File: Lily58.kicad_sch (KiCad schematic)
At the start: 30 parts, among them J1 USB_C_Receptacle, J2 USB_C_Receptacle, Q1 2N7002, Q2 2N7002, Q3 2N7002, Q4 2N7002, U1 ESP32-S3-WROOM-2, U2 TPS63001, U3 BQ24090DGQ, Y1 Crystal_GND24

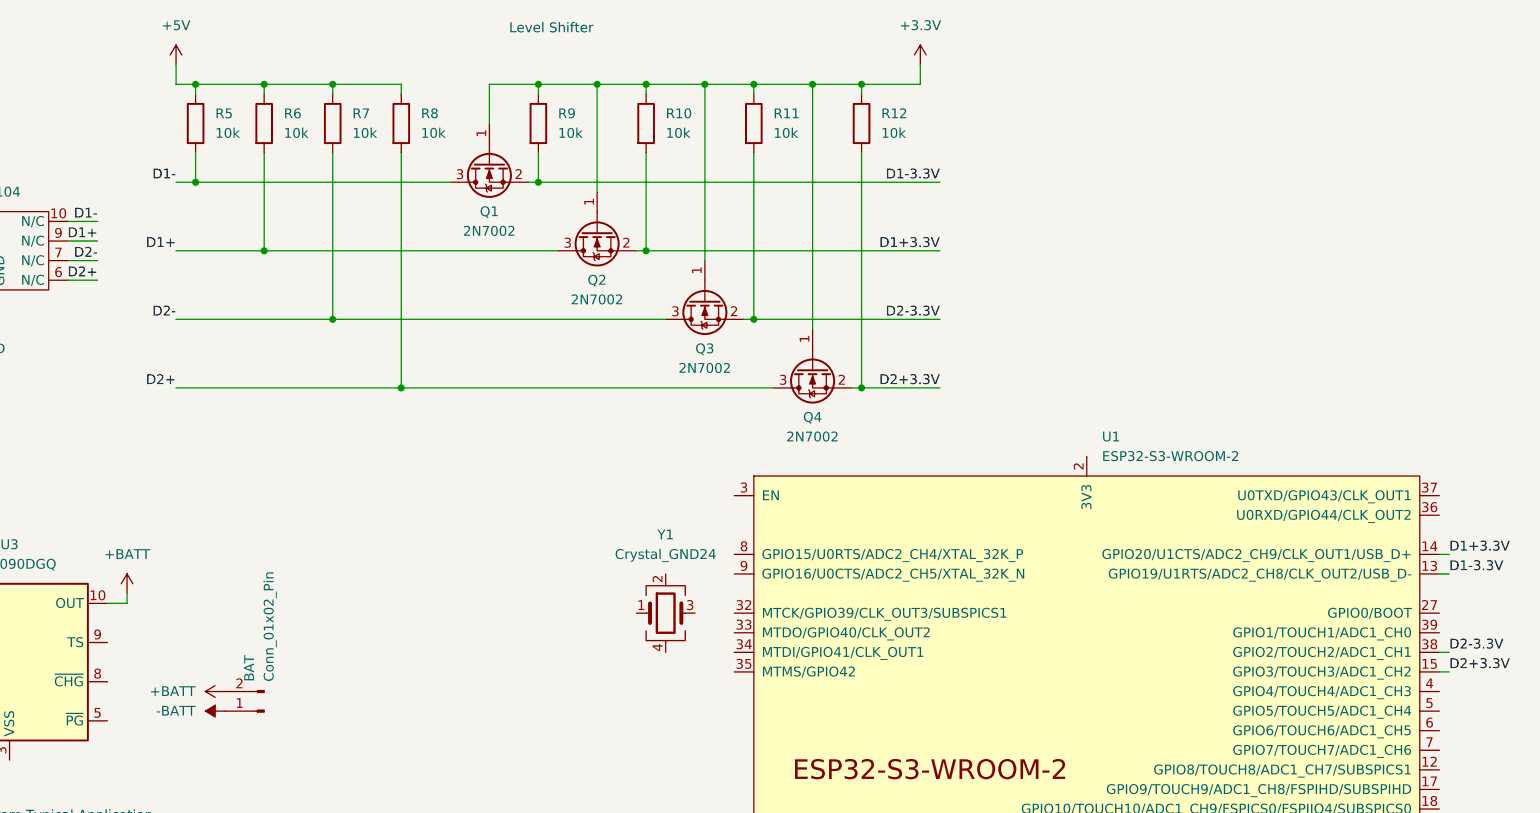
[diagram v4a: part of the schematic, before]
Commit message: removed unnecessary level shifter since data lines are 3V3 already
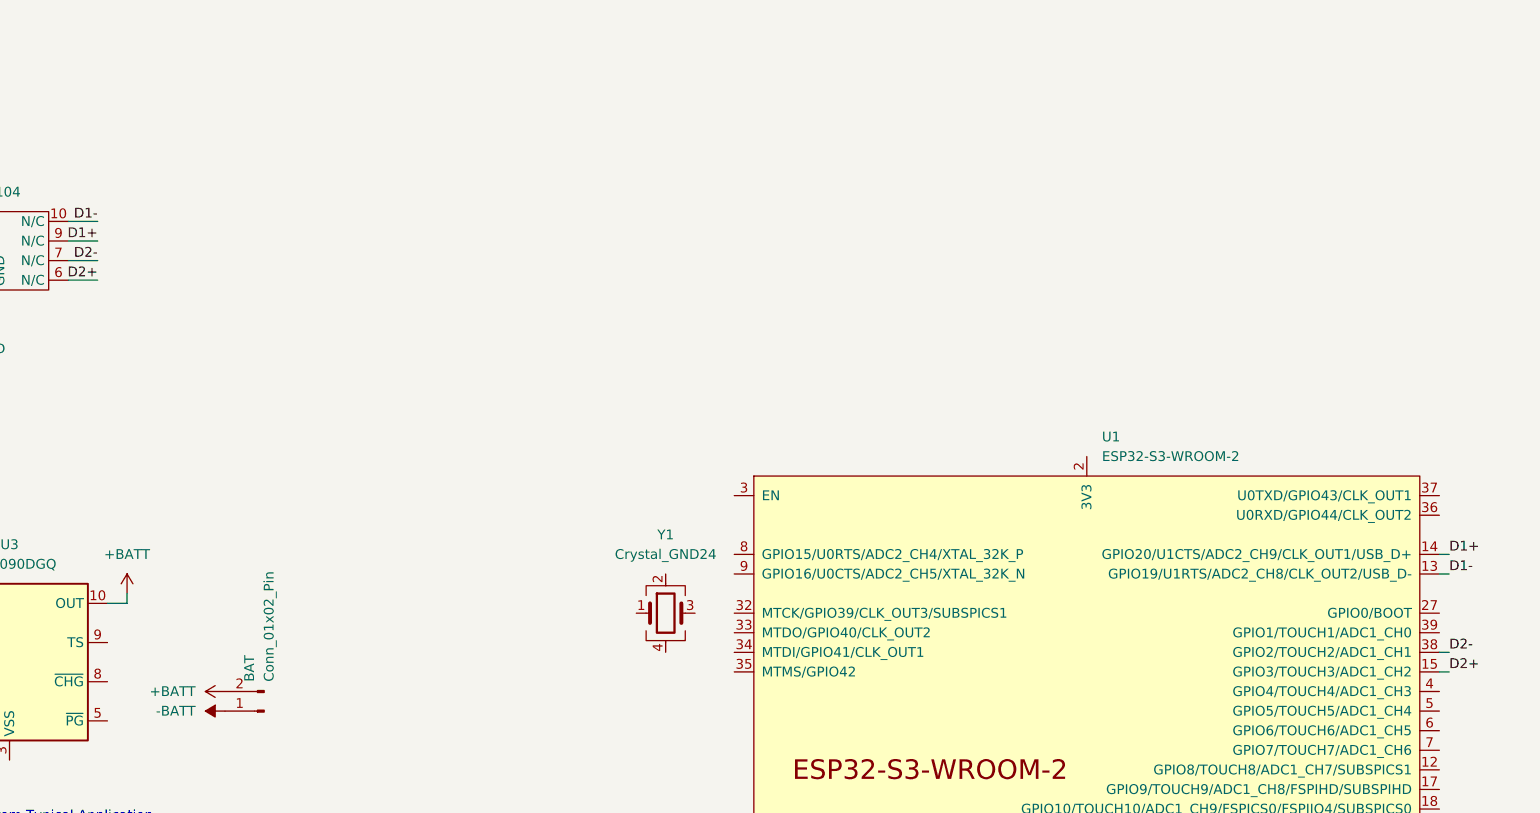
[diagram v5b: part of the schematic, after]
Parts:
- removed Q1, Q2, Q3, Q4: 2N7002, Package_TO_SOT_SMD:SOT-23, symbol Transistor_FET:2N7002
- removed R10, R11, R12, R5, R6, R7, R8, R9: 10k, symbol Device:R
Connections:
- net D1+3.3V is gone; now on net D1+: U1.14 (GPIO20/U1CTS/ADC2_CH9/CLK_OUT1/USB_D+)
- net D1-3.3V is gone; now on net D1-: U1.13 (GPIO19/U1RTS/ADC2_CH8/CLK_OUT2/USB_D-)
- net D2+3.3V is gone; now on net D2+: U1.15 (GPIO3/TOUCH3/ADC1_CH2)
- net D2-3.3V is gone; now on net D2-: U1.38 (GPIO2/TOUCH2/ADC1_CH1)
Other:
- note removed: "Level Shifter"

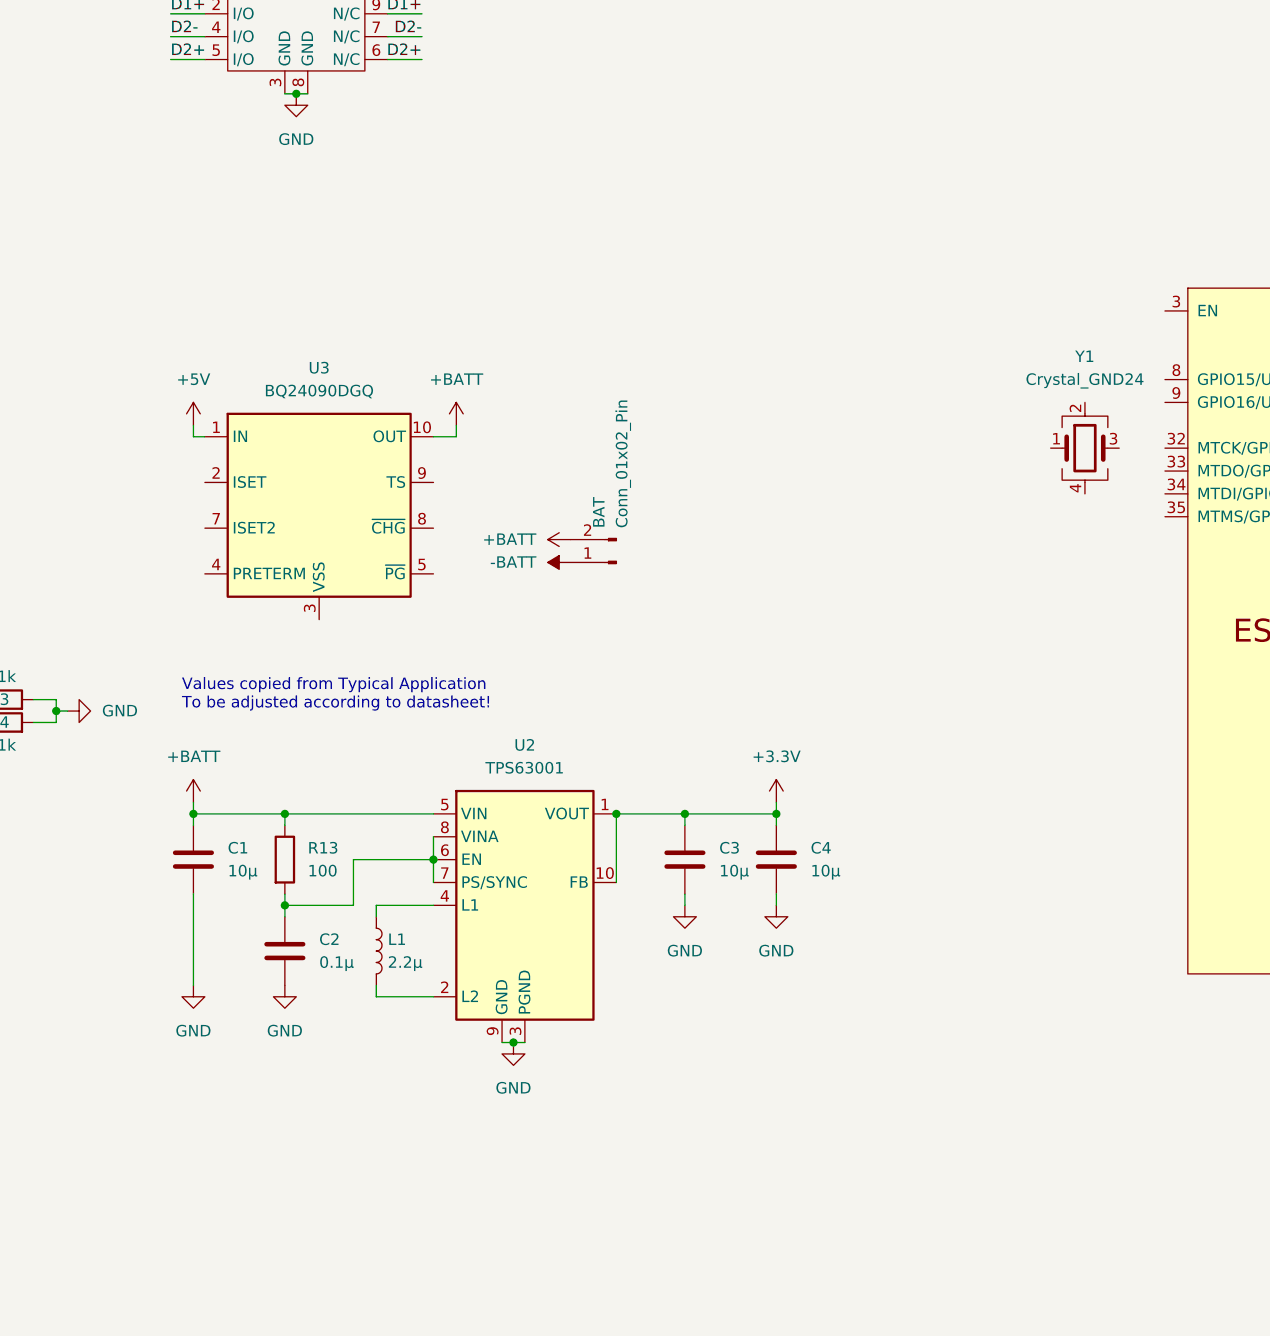
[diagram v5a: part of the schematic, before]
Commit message: added buck-boost-converters and corrected passive components
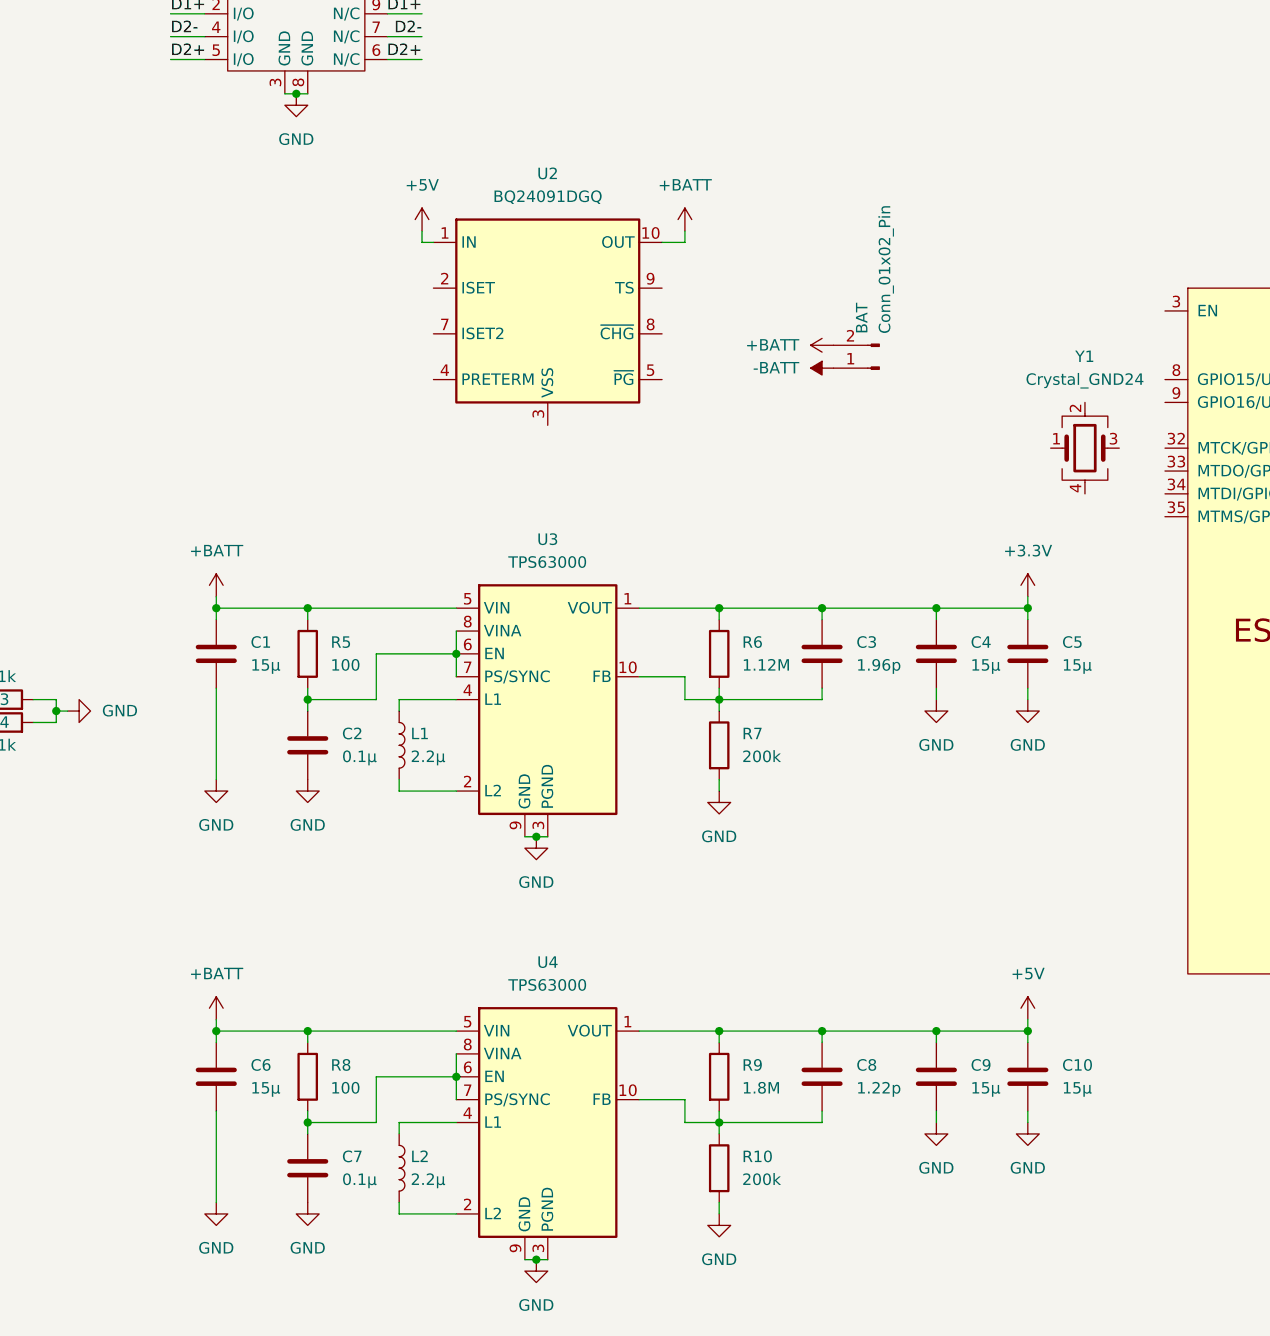
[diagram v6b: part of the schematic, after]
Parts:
- removed R13: 100, symbol Device:R
- added C10, C6, C9: 15µ, symbol Device:C
- added C3: 1.96p, symbol Device:C
- added C7: 0.1µ, symbol Device:C
- added C8: 1.22p, symbol Device:C
- added L2: 2.2µ, symbol Device:L
- added R10, R7: 200k, symbol Device:R
- added R5, R8: 100, symbol Device:R
- added R6: 1.12M, symbol Device:R
- added R9: 1.8M, symbol Device:R
- added U4: TPS63000, Package_SON:Texas_DRC0010J_ThermalVias, symbol Regulator_Switching:TPS63001
- C1: value 10µ -> 15µ
- C4: renamed from C3; value 10µ -> 15µ
- C5: renamed from C4; value 10µ -> 15µ
- U2: renamed from U3; value BQ24090DGQ -> BQ24091DGQ
- U3: renamed from U2; value TPS63001 -> TPS63000
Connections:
- net +3.3V: now also C3.1, R6.1; no longer U3.10 (FB)
- net +5V: now also C10.1, C8.1, C9.1, R9.1, U4.1 (VOUT)
- net +BATT: now also C6.1, R5.1, R8.1, U4.5 (VIN)
- net GND: now also C10.2, C6.2, C7.2, C9.2, R10.2, R7.2, U4.11 (PGND), U4.3 (PGND), U4.9 (GND)
- net at C2.1, U3.6 (EN), U3.7 (PS/SYNC)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: now also R5.2
- new net: L2.1, U4.4 (L1)
- new net: L2.2, U4.2 (L2)
- new net: C8.2, R10.1, R9.2, U4.10 (FB)
- new net: C7.1, R8.2, U4.6 (EN), U4.7 (PS/SYNC), U4.8 (VINA)
- new net: C3.2, R6.2, R7.1, U3.10 (FB)
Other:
- note removed: "Values copied from Typical Application To be adjusted according to datasheet!"
- moved on the sheet: BAT, C1, C2, C4, C5, L1, U2, U3

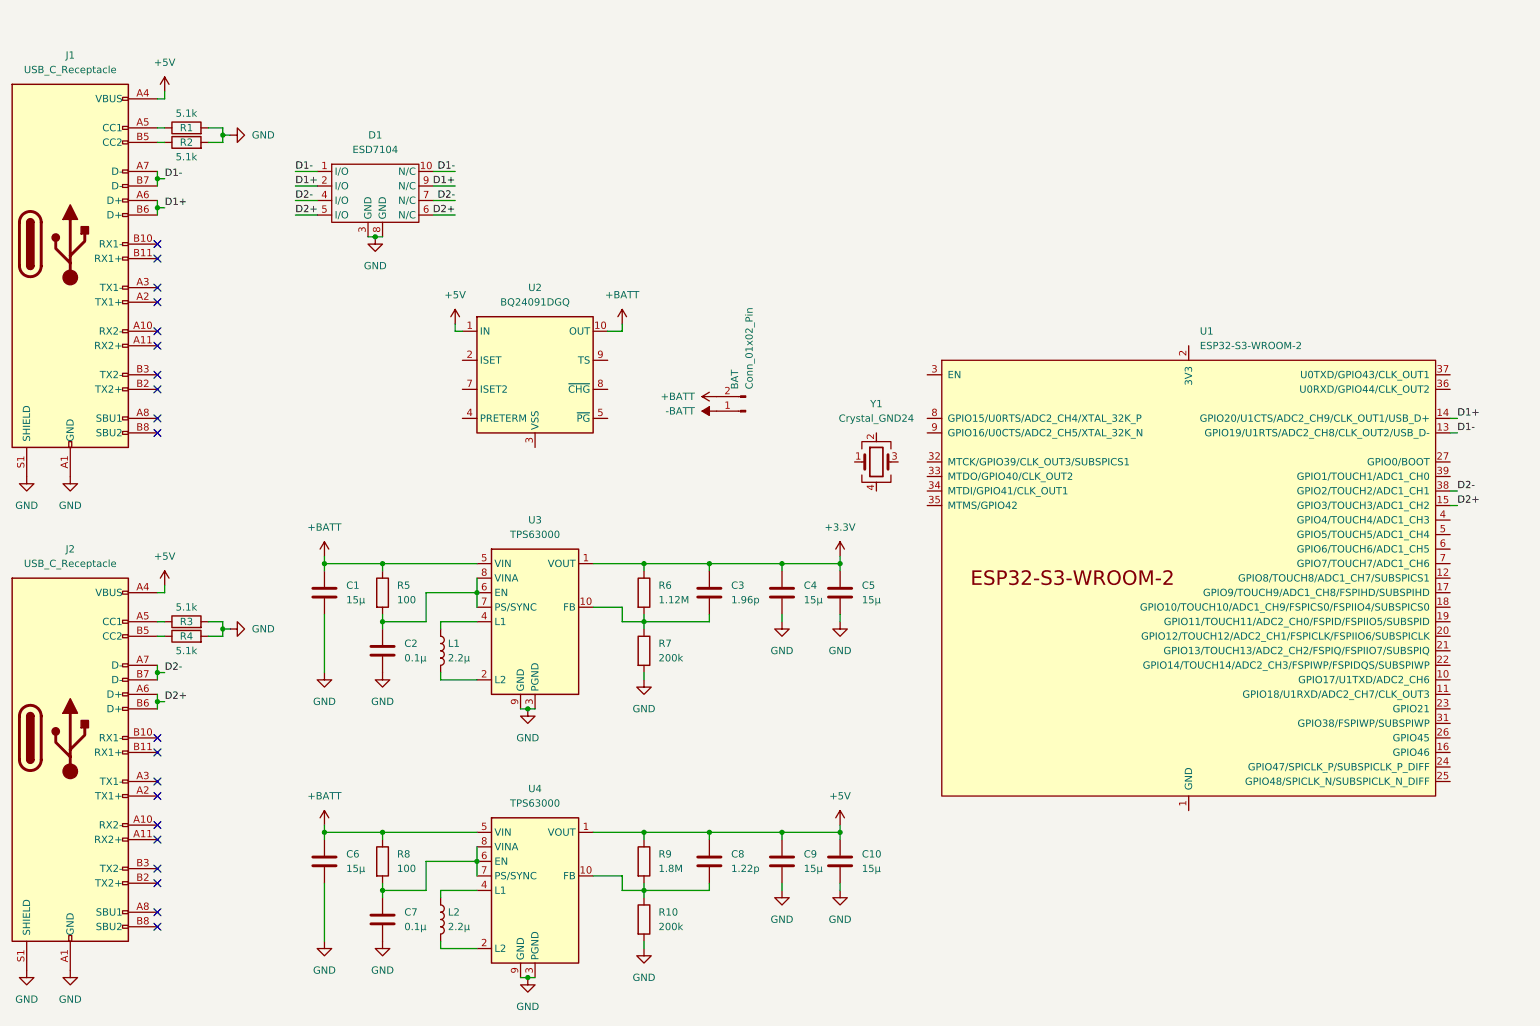
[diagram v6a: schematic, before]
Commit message: added battery charger circuit; passive components still temporary
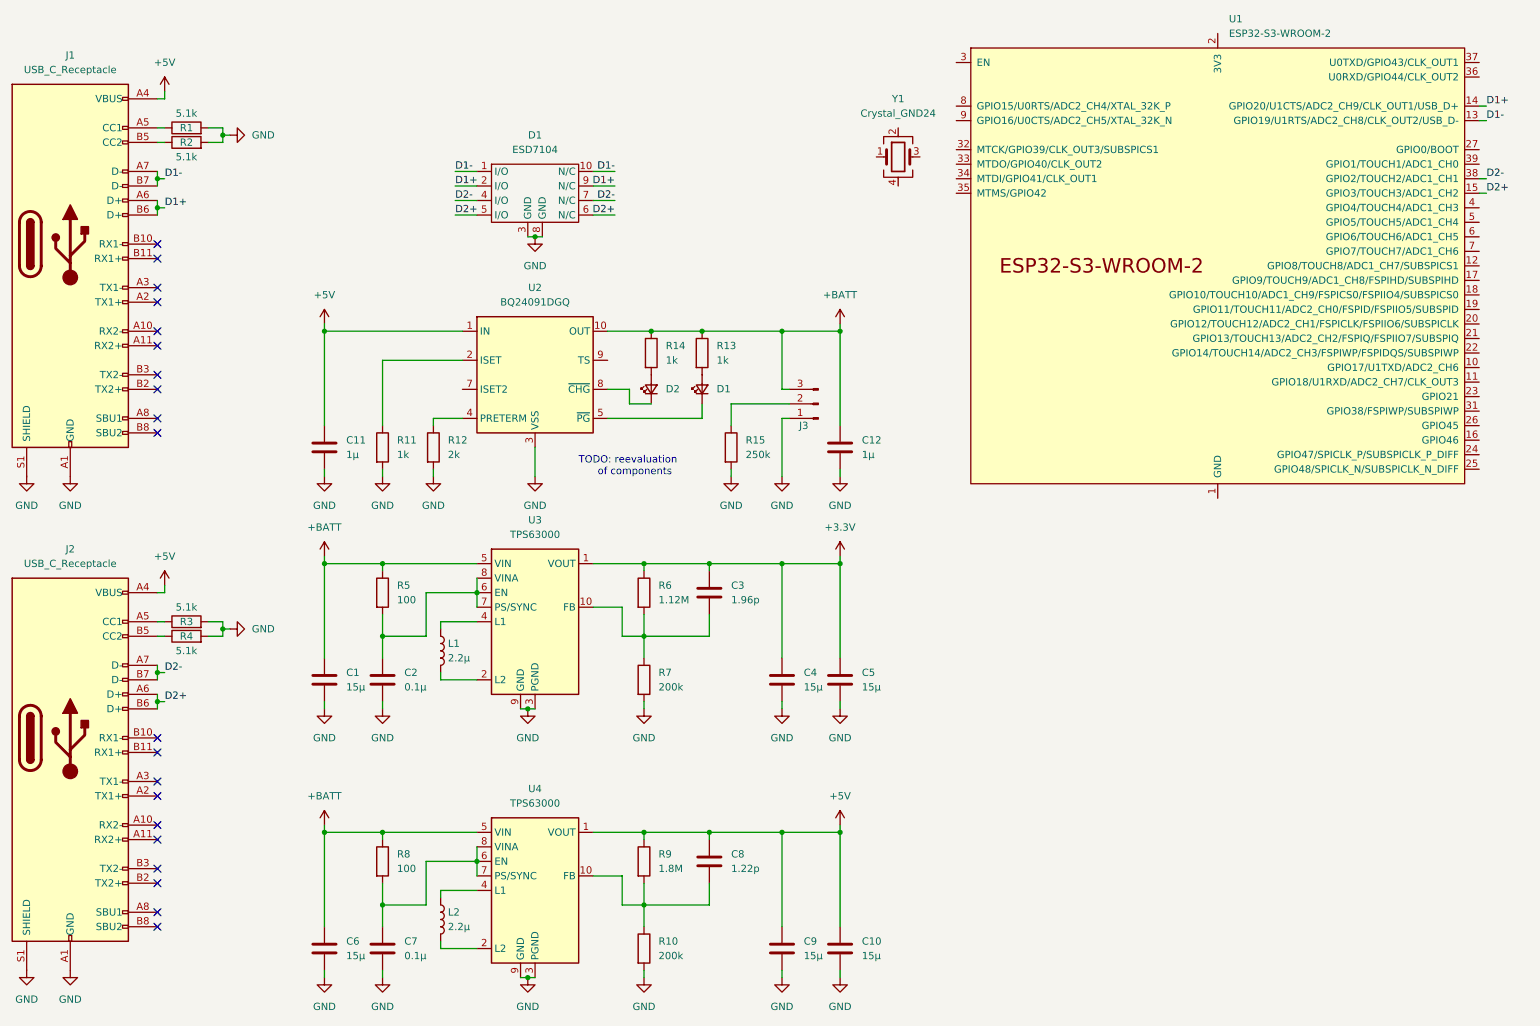
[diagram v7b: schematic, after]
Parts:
- removed BAT: Conn_01x02_Pin, Connector_JST:JST_EH_B2B-EH-A_1x02_P2.50mm_Vertical, symbol Connector:Conn_01x02_Pin
- added C11, C12: 1µ, symbol Device:C
- added D1, D2: LED_Small, symbol Device:LED_Small
- added J3: Conn_01x03_Pin, symbol Connector:Conn_01x03_Pin
- added R11, R13, R14: 1k, symbol Device:R
- added R12: 2k, symbol Device:R
- added R15: 250k, symbol Device:R
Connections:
- net +5V: now also C11.1
- net +BATT: now also C12.1, J3.3 (Pin_3), R13.1, R14.1
- net GND: now also U2.11 (VSS), U2.3 (VSS), C11.2, C12.2, J3.1 (Pin_1), R11.2, R12.2, R15.2
- net at U2.2 (ISET): now also R11.1
- net at U2.4 (PRETERM): now also R12.1
- net at U2.5 (~{PG}): now also D1.1 (K)
- net at U2.8 (~{CHG}): now also D2.1 (K)
- new net: D1.2 (A), R13.2
- new net: J3.2 (Pin_2), R15.1
- new net: D2.2 (A), R14.2
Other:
- note added: "TODO: reevaluation of components"
- moved on the sheet: C1, C10, C2, C4, C5, C6, C7, C9, D1, R10, R7, U1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

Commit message: changed dataline labeling
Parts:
- removed U1: ESP32-S3-WROOM-2, PCM_Espressif:ESP32-S3-WROOM-2, symbol PCM_Espressif:ESP32-S3-WROOM-2
- added U4: ESP32-S3-WROOM-1, PCM_Espressif:ESP32-S3-WROOM-1, symbol PCM_Espressif:ESP32-S3-WROOM-1
- renumbered U2 to U1, U3 to U2, U4 to U3
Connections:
- net D1+ renamed USB1_D+
- net USB1_D+: now also U4.14 (GPIO20/U1CTS/ADC2_CH9/CLK_OUT1/USB_D+)
- net D1- renamed USB1_D-
- net USB1_D-: now also U4.13 (GPIO19/U1RTS/ADC2_CH8/CLK_OUT2/USB_D-)
- net D2+ renamed USB2_D+
- net USB2_D+: now also U4.15 (GPIO3/TOUCH3/ADC1_CH2)
- net D2- renamed USB2_D-
- net USB2_D-: now also U4.38 (GPIO2/TOUCH2/ADC1_CH1)
- new net: U4.1 (GND), U4.40 (GND), U4.41 (GND)
